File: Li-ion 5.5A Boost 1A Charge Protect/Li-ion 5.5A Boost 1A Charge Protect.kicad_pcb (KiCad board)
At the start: 2 copper layers, 51.5 x 32 mm, 55 parts, among them J1 USB_C_FEMALE, Q1 BUK6D30-40E, SW1 SW_DPST, U1 AP9101CK6, U2 ECH8695R-TL-W, U3 MCP73833T, U4 PAM2423AECADJR

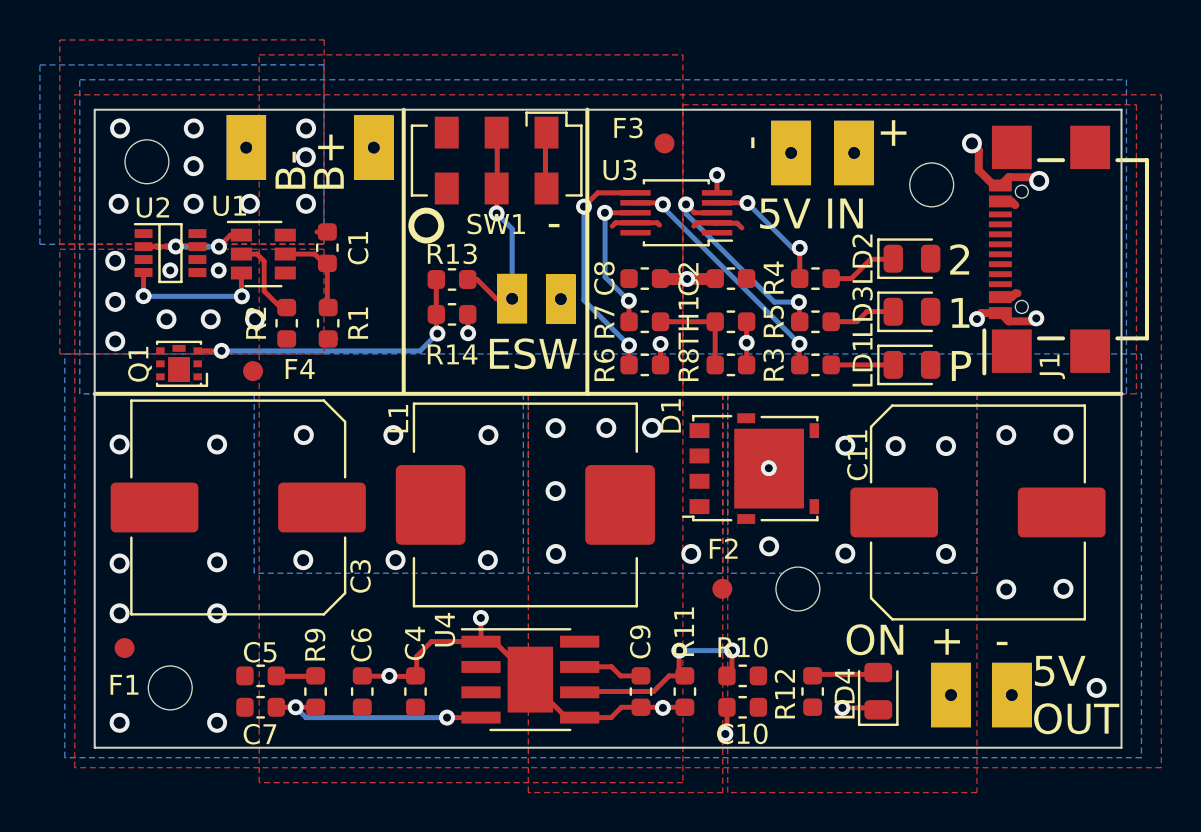
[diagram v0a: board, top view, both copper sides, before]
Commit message: Renaming 5A to 5.5A
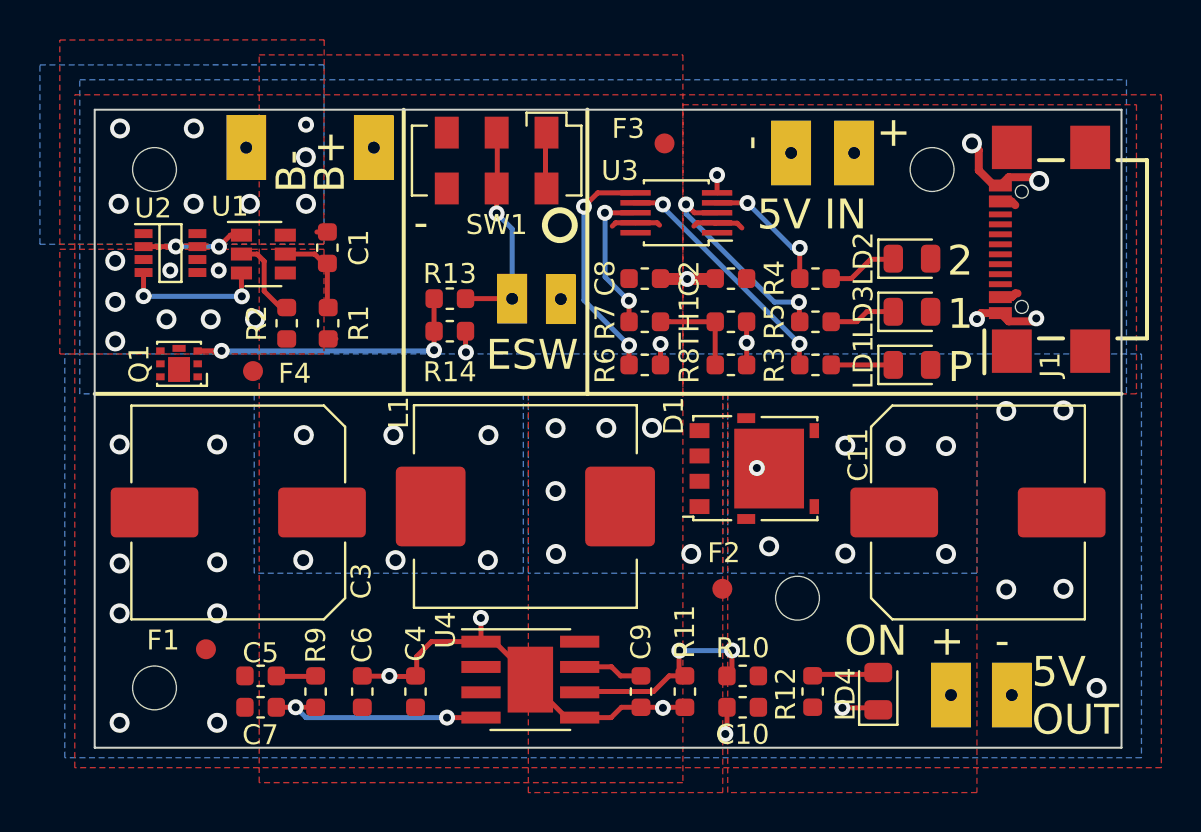
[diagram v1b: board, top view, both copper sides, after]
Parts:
- added LG1: Logo, Logo_LE:Ikosy-Logo_Type1_10.3x2mm_SilkScreen, B.Cu at (145.9, 76.9)
- added LG2: Logo, Logo_LE:OSHW-Symbol_3mm_Silkscreen, B.Cu at (136.5, 76.9)
- added LG3: Logo, Logo_LE:KiCad-Logo3_3mm_SilkScreen, B.Cu at (128.8, 76.9)
- D1: value NTS12120EMFST1G -> 120V 12A
- moved F1 4.08 mm to (105.6, 95.1)
- moved R13 0.97 mm to (117.8, 77.5)
- moved R14 0.85 mm to (117.8, 79.1)
- moved H1 0.79 mm to (103.0, 97.0)
- moved H3 0.77 mm to (142.0, 71.0)
- moved H4 0.54 mm to (103.0, 71.0)
- moved H2 0.46 mm to (135.2, 92.5)
- moved C3 0.25 mm to (107.2, 88.2)
- moved L1 0.08 mm to (121.6, 87.9)
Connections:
- J1 pad A5: Net-(J1-PadA5) -> (no net)
- J1 pad A6: Net-(J1-PadA6) -> (no net)
- J1 pad A7: Net-(J1-PadA7) -> (no net)
- J1 pad A8: Net-(J1-PadA8) -> (no net)
- J1 pad B5: Net-(J1-PadB5) -> (no net)
- J1 pad B6: Net-(J1-PadB6) -> (no net)
- J1 pad B7: Net-(J1-PadB7) -> (no net)
- J1 pad B8: Net-(J1-PadB8) -> (no net)
- J1 pad S1: Net-(J1-PadS1) -> (no net)
- J1 pad S2: Net-(J1-PadS2) -> (no net)
- J1 pad S3: Net-(J1-PadS3) -> (no net)
- J1 pad S4: Net-(J1-PadS4) -> (no net)
- U1 pad 4: Net-(U1-Pad4) -> (no net)
- U2 pad 5: Net-(U2-Pad5) -> (no net)
- U2 pad 6: Net-(U2-Pad6) -> (no net)
- U2 pad 7: Net-(U2-Pad7) -> (no net)
- U2 pad 8: Net-(U2-Pad8) -> (no net)
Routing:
- net Net-(Q1-Pad3): track 15.1 -> 14.5 mm
- net /BATT-: vias 9 -> 8

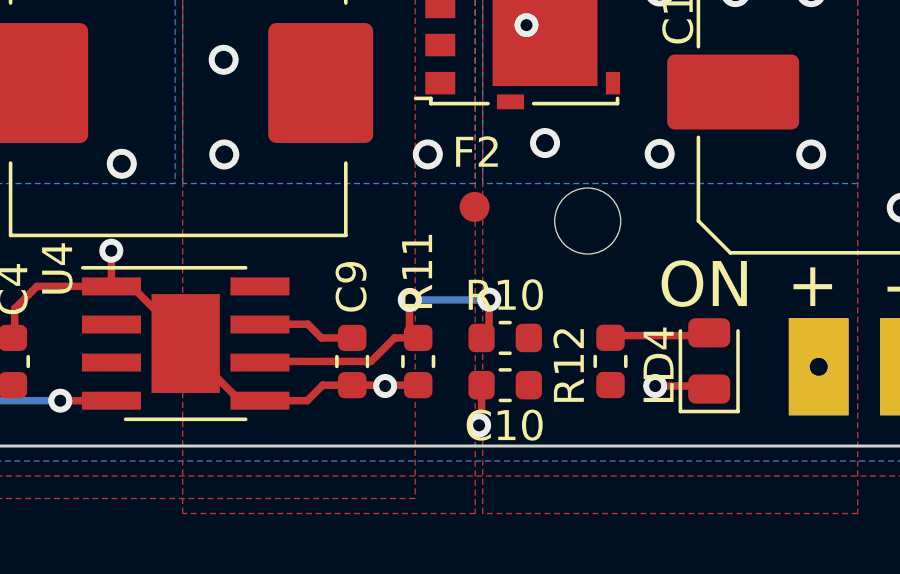
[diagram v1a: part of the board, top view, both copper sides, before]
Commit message: Update Li-ion 5.5A Boost 1A Charge Protect.kicad_pcb
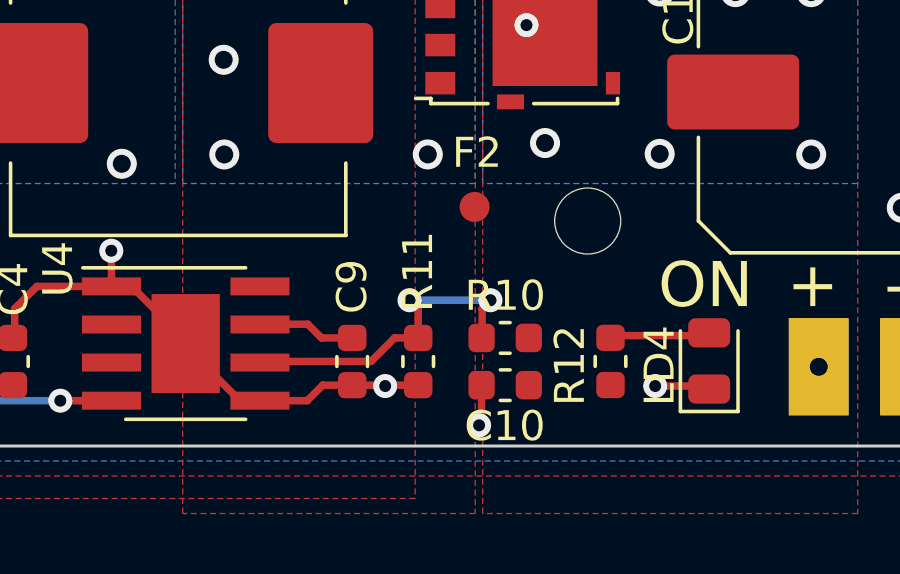
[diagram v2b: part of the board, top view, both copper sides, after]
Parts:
- moved LG1 0.75 mm to (145.9, 76.2)
- moved LG2 0.75 mm to (136.5, 76.2)
- moved LG3 0.75 mm to (128.8, 76.1)
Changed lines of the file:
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@@
     (thickness 1.6)
     (drawings 71)
-    (tracks 251)
+    (tracks 253)
     (zones 0)
     (modules 58)
@@
   (page A)
   (layers
-    (0 F.Cu signal)
-    (31 B.Cu signal)
-    (32 B.Adhes user)
-    (33 F.Adhes user)
-    (34 B.Paste user)
-    (35 F.Paste user)
+    (0 F.Cu signal hide)
+    (31 B.Cu signal hide)
+    (32 B.Adhes user hide)
+    (33 F.Adhes user hide)
+    (34 B.Paste user hide)
+    (35 F.Paste user hide)
     (36 B.SilkS user)
-    (37 F.SilkS user)
-    (38 B.Mask user)
-    (39 F.Mask user)
+    (37 F.SilkS user hide)
+    (38 B.Mask user hide)
+    (39 F.Mask user hide)
     (40 Dwgs.User user hide)
     (41 Cmts.User user hide)
@@
     (add_net GND)
     (add_net "Net-(C5-Pad1)")
-    (add_net "Net-(J1-PadA5)")
-    (add_net "Net-(J1-PadA6)")
-    (add_net "Net-(J1-PadA7)")
-    (add_net "Net-(J1-PadA8)")
-    (add_net "Net-(J1-PadB5)")
-    (add_net "Net-(J1-PadB6)")
-    (add_net "Net-(J1-PadB7)")
-    (add_net "Net-(J1-PadB8)")
-    (add_net "Net-(J1-PadS1)")
-    (add_net "Net-(J1-PadS2)")
-    (add_net "Net-(J1-PadS3)")
-    (add_net "Net-(J1-PadS4)")
     (add_net "Net-(LD1-Pad1)")
     (add_net "Net-(LD2-Pad1)")
@@
     (add_net "Net-(U1-Pad1)")
     (add_net "Net-(U1-Pad3)")
-    (add_net "Net-(U1-Pad4)")
-    (add_net "Net-(U2-Pad5)")
-    (add_net "Net-(U2-Pad6)")
-    (add_net "Net-(U2-Pad7)")
-    (add_net "Net-(U2-Pad8)")
   )
   (net_class "High Power" ""
@@
   )
   (module Logo_LE:Ikosy-Logo_Type1_10.3x2mm_SilkScreen (layer B.Cu)
-    (at 145.86 76.92 180)
+    (at 145.86 76.17 180)
     (attr virtual)
-    (fp_text reference LG1 (at 0 2.1) (layer B.SilkS) hide
+    (fp_text reference LG1 (at 0 2.1) (layer F.Fab) hide
       (effects (font (size 1.524 1.524) (thickness 0.3)) (justify mirror))
     )
-    (fp_text value Logo (at 0 -2.3) (layer B.SilkS) hide
+    (fp_text value Logo (at 0 -2.3) (layer F.Fab) hide
       (effects (font (size 1.524 1.524) (thickness 0.3)) (justify mirror))
     )
@@
   )
   (module Logo_LE:KiCad-Logo3_3mm_SilkScreen (layer B.Cu)
-    (at 128.77 76.89 180)
-    (fp_text reference LG3 (at 0 2.6) (layer B.SilkS) hide
+    (at 128.77 76.14 180)
+    (fp_text reference LG3 (at 0 2.6) (layer F.Fab) hide
       (effects (font (size 1.524 1.524) (thickness 0.3)) (justify mirror))
     )
-    (fp_text value Logo (at 0 -3) (layer B.SilkS) hide
+    (fp_text value Logo (at 0 -3) (layer F.Fab) hide
       (effects (font (size 1.524 1.524) (thickness 0.3)) (justify mirror))
     )
@@
   )
   (module Logo_LE:OSHW-Symbol_3mm_Silkscreen (layer B.Cu)
-    (at 136.511603 76.91898 180)
+    (at 136.511603 76.16898 180)
     (attr virtual)
     (fp_text reference LG2 (at -0.13 2.1) (layer B.Fab) hide
@@
   (segment (start 129.6 96.3965) (end 128.8135 96.3965) (width 0.25) (layer F.Cu) (net 12))
   (segment (start 128.8135 96.3965) (end 128.03 97.18) (width 0.25) (layer F.Cu) (net 12))
-  (via (at 131.97 95.12) (size 0.8) (drill 0.4) (layers F.Cu B.Cu) (net 12))
-  (segment (start 131.9625 96.3965) (end 131.9625 95.1275) (width 0.25) (layer F.Cu) (net 12))
-  (via (at 129.32 95.13) (size 0.8) (drill 0.4) (layers F.Cu B.Cu) (net 12))
-  (segment (start 129.31 96.3965) (end 129.31 95.14) (width 0.25) (layer F.Cu) (net 12))
-  (segment (start 129.33 95.13) (end 131.97 95.13) (width 0.25) (layer B.Cu) (net 12))
+  (segment (start 131.73 95.42) (end 131.73 96.42) (width 0.25) (layer F.Cu) (net 12))
+  (via (at 132.01 95.14) (size 0.8) (drill 0.4) (layers F.Cu B.Cu) (net 12))
+  (segment (start 132.01 95.14) (end 131.73 95.42) (width 0.25) (layer F.Cu) (net 12))
+  (via (at 129.31 95.14) (size 0.8) (drill 0.4) (layers F.Cu B.Cu) (net 12))
+  (segment (start 129.31 95.14) (end 132.01 95.14) (width 0.25) (layer B.Cu) (net 12))
+  (segment (start 129.6 95.43) (end 129.6 96.35) (width 0.25) (layer F.Cu) (net 12))
+  (segment (start 129.31 95.14) (end 129.6 95.43) (width 0.25) (layer F.Cu) (net 12))
   (via (at 137.65 90.262) (size 1) (drill 0.6) (layers F.Cu B.Cu) (net 13))
   (via (at 140.175 84.87) (size 1) (drill 0.6) (layers F.Cu B.Cu) (net 13))
